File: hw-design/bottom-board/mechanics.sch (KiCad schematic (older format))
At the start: 8 parts

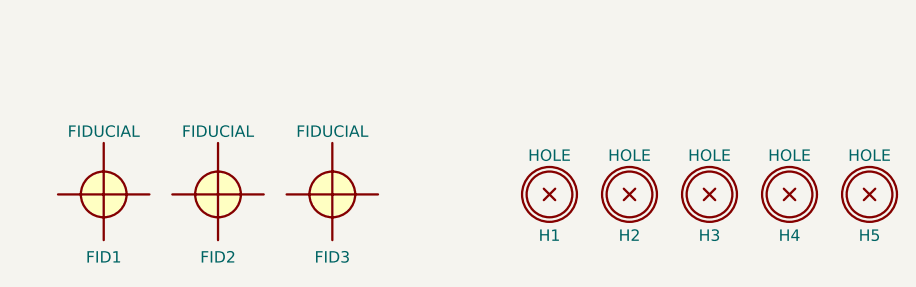
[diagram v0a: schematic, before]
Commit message: changed a bottomboard to a minimal HMI testing unit
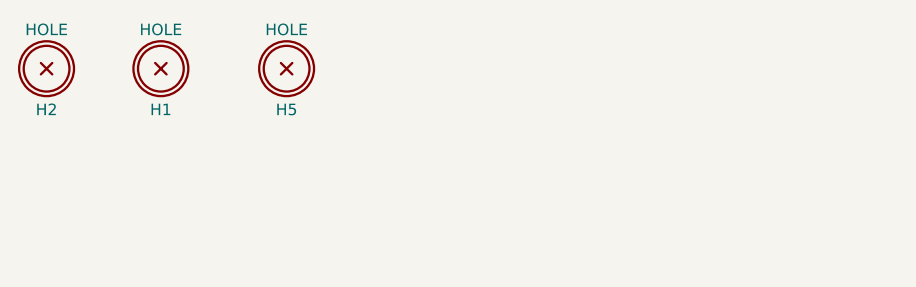
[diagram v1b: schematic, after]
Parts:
- removed FID1, FID2, FID3: FIDUCIAL, footprints:fiducial_in-circuit, symbol bottom-board-rescue:FIDUCIAL-local-components
- removed H3, H4: HOLE, footprints:Hole_3.5mm, symbol bottom-board-rescue:HOLE-local-components
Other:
- moved on the sheet: H2, H5
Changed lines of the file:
@@
 EESchema Schematic File Version 4
 LIBS:bottom-board-cache
-EELAYER 26 0
+EELAYER 29 0
 EELAYER END
 $Descr A4 11693 8268
 encoding utf-8
-Sheet 12 12
-Title ""
+Sheet 5 7
+Title "MOD Duo -HMI testing board"
 Date ""
-Rev ""
-Comp ""
-Comment1 ""
-Comment2 ""
-Comment3 ""
-Comment4 ""
+Rev "1.0"
+Comp "MOD Devices GmbH"
+Comment1 "Controller board Tester"
+Comment2 "used for the MOD Duo"
+Comment3 "or MOD Duo X controller"
+Comment4 "Compatible w/ Marsboard SoM"
 $EndDescr
-$Comp
-L bottom-board-rescue:FIDUCIAL-local-components FID1
-U 1 1 55FC074E
-P 1400 1400
-AR Path="/55FC074E" Ref="FID1"  Part="1"
-AR Path="/55FC02AF/55FC074E" Ref="FID1"  Part="1"
-F 0 "FID1" H 1400 1125 50  0000 C CNN
-F 1 "FIDUCIAL" H 1400 1675 50  0000 C CNN
-F 2 "footprints:fiducial_in-circuit" H 1400 1400 60  0001 C CNN
-F 3 "" H 1400 1400 60  0000 C CNN
-	1    1400 1400
-	1    0    0    -1
-$EndComp
-$Comp
-L bottom-board-rescue:HOLE-local-components H1
-U 1 1 55FC0943
-P 3350 1400
-AR Path="/55FC0943" Ref="H1"  Part="1"
-AR Path="/55FC02AF/55FC0943" Ref="H1"  Part="1"
-F 0 "H1" H 3350 1220 50  0000 C CNN
-F 1 "HOLE" H 3350 1570 50  0000 C CNN
-F 2 "footprints:Hole_3.5mm" H 3350 1400 60  0001 C CNN
-F 3 "" H 3350 1400 60  0000 C CNN
-	1    3350 1400
-	1    0    0    -1
-$EndComp
-$Comp
-L bottom-board-rescue:FIDUCIAL-local-components FID2
-U 1 1 55FC1F87
-P 1900 1400
-AR Path="/55FC1F87" Ref="FID2"  Part="1"
-AR Path="/55FC02AF/55FC1F87" Ref="FID2"  Part="1"
-F 0 "FID2" H 1900 1125 50  0000 C CNN
-F 1 "FIDUCIAL" H 1900 1675 50  0000 C CNN
-F 2 "footprints:fiducial_in-circuit" H 1900 1400 60  0001 C CNN
-F 3 "" H 1900 1400 60  0000 C CNN
-	1    1900 1400
-	1    0    0    -1
-$EndComp
-$Comp
-L bottom-board-rescue:FIDUCIAL-local-components FID3
-U 1 1 55FC1FBF
-P 2400 1400
-AR Path="/55FC1FBF" Ref="FID3"  Part="1"
-AR Path="/55FC02AF/55FC1FBF" Ref="FID3"  Part="1"
-F 0 "FID3" H 2400 1125 50  0000 C CNN
-F 1 "FIDUCIAL" H 2400 1675 50  0000 C CNN
-F 2 "footprints:fiducial_in-circuit" H 2400 1400 60  0001 C CNN
-F 3 "" H 2400 1400 60  0000 C CNN
-	1    2400 1400
-	1    0    0    -1
-$EndComp
 $Comp
 L bottom-board-rescue:HOLE-local-components H2
 U 1 1 55FC2212
-P 3700 1400
+P 1150 850
 AR Path="/55FC2212" Ref="H2"  Part="1"
 AR Path="/55FC02AF/55FC2212" Ref="H2"  Part="1"
-F 0 "H2" H 3700 1220 50  0000 C CNN
-F 1 "HOLE" H 3700 1570 50  0000 C CNN
-F 2 "footprints:Hole_3.5mm" H 3700 1400 60  0001 C CNN
-F 3 "" H 3700 1400 60  0000 C CNN
-	1    3700 1400
-	1    0    0    -1
-$EndComp
-$Comp
-L bottom-board-rescue:HOLE-local-components H3
-U 1 1 55FC224E
-P 4050 1400
-AR Path="/55FC224E" Ref="H3"  Part="1"
-AR Path="/55FC02AF/55FC224E" Ref="H3"  Part="1"
-F 0 "H3" H 4050 1220 50  0000 C CNN
-F 1 "HOLE" H 4050 1570 50  0000 C CNN
-F 2 "footprints:Hole_3.5mm" H 4050 1400 60  0001 C CNN
-F 3 "" H 4050 1400 60  0000 C CNN
-	1    4050 1400
-	1    0    0    -1
-$EndComp
-$Comp
-L bottom-board-rescue:HOLE-local-components H4
-U 1 1 55FC227A
-P 4400 1400
-AR Path="/55FC227A" Ref="H4"  Part="1"
-AR Path="/55FC02AF/55FC227A" Ref="H4"  Part="1"
-F 0 "H4" H 4400 1220 50  0000 C CNN
-F 1 "HOLE" H 4400 1570 50  0000 C CNN
-F 2 "footprints:Hole_3.5mm" H 4400 1400 60  0001 C CNN
-F 3 "" H 4400 1400 60  0000 C CNN
-	1    4400 1400
+F 0 "H2" H 1150 670 50  0000 C CNN
+F 1 "HOLE" H 1150 1020 50  0000 C CNN
+F 2 "footprints:Hole_3.5mm" H 1150 850 60  0001 C CNN
+F 3 "" H 1150 850 60  0000 C CNN
+	1    1150 850
 	1    0    0    -1
 $EndComp
@@
 L bottom-board-rescue:HOLE-local-components H5
 U 1 1 55FC22B0
-P 4750 1400
+P 2200 850
 AR Path="/55FC22B0" Ref="H5"  Part="1"
 AR Path="/55FC02AF/55FC22B0" Ref="H5"  Part="1"
-F 0 "H5" H 4750 1220 50  0000 C CNN
-F 1 "HOLE" H 4750 1570 50  0000 C CNN
-F 2 "footprints:Hole_3.5mm" H 4750 1400 60  0001 C CNN
-F 3 "" H 4750 1400 60  0000 C CNN
-	1    4750 1400
+F 0 "H5" H 2200 670 50  0000 C CNN
+F 1 "HOLE" H 2200 1020 50  0000 C CNN
+F 2 "footprints:Hole_3.5mm" H 2200 850 60  0001 C CNN
+F 3 "" H 2200 850 60  0000 C CNN
+	1    2200 850
 	1    0    0    -1
 $EndComp
+$Comp
+L bottom-board-rescue:HOLE-local-components H?
+U 1 1 5D06CB0A
+P 1650 850
+AR Path="/5D06CB0A" Ref="H?"  Part="1"
+AR Path="/55FC02AF/5D06CB0A" Ref="H1"  Part="1"
+F 0 "H1" H 1650 670 50  0000 C CNN
+F 1 "HOLE" H 1650 1020 50  0000 C CNN
+F 2 "footprints:Hole_3.5mm" H 1650 850 60  0001 C CNN
+F 3 "" H 1650 850 60  0000 C CNN
+	1    1650 850
+	1    0    0    -1
+$EndComp
